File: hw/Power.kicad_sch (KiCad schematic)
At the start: 1 part, among them J4 CONN_BAT

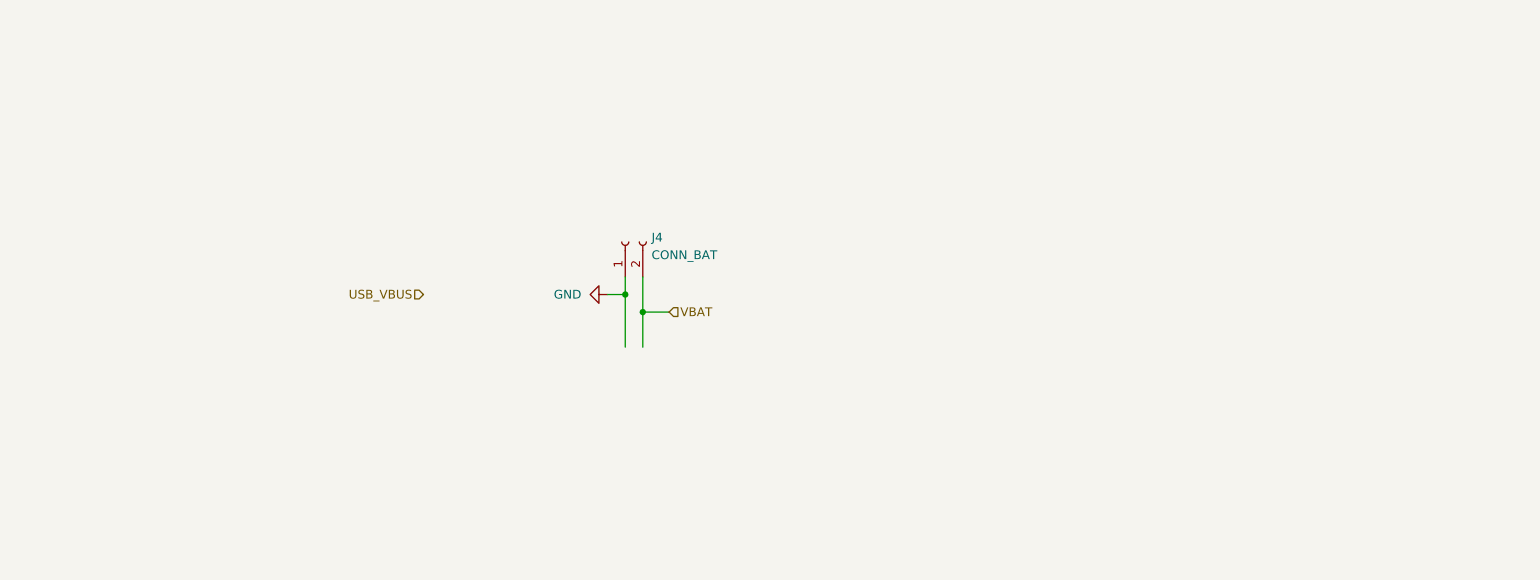
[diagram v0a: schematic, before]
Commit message: Replace case, start on Power stages
I've replaced the case STL with one that's better in every way, it prints faster, doesn't need supports, and the holder for the diffuser is better,

I may still tweak the design but I'm happy with it for now.
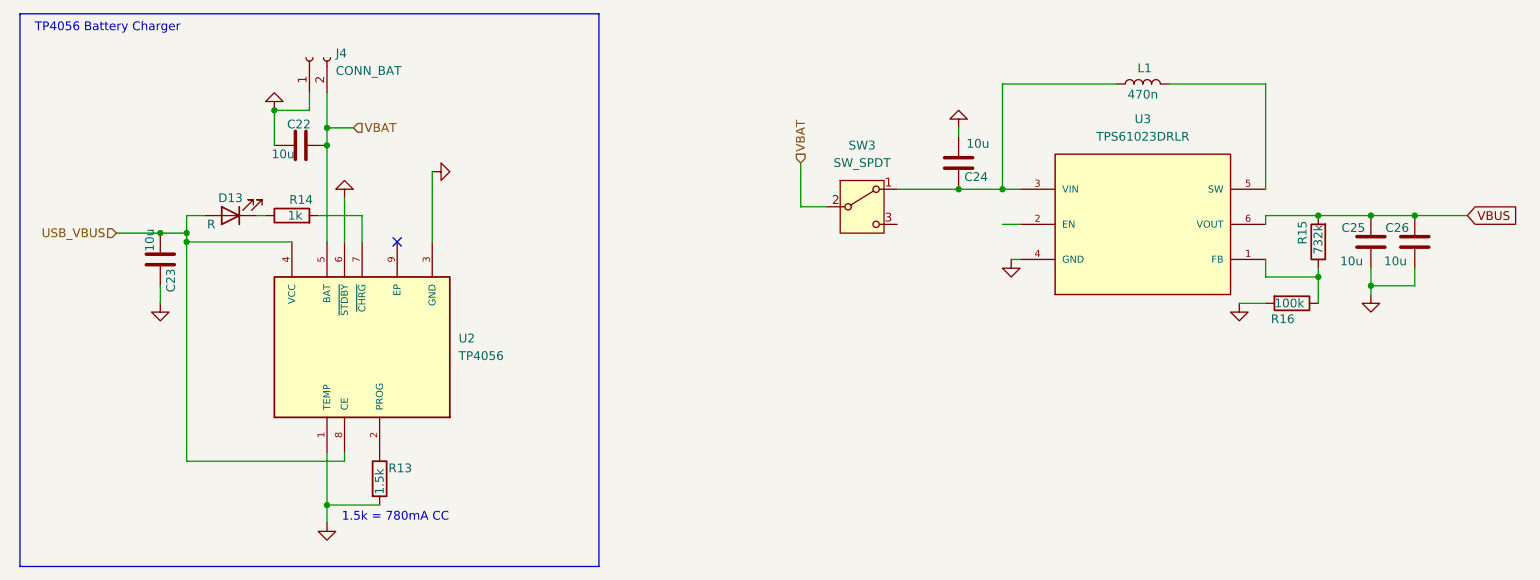
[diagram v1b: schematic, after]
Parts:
- added C22, C23, C24, C25, C26: 10u, symbol Device:C
- added D13: R, symbol Device:LED
- added L1: 470n, symbol Device:L
- added R13: 1.5k, symbol Device:R
- added R14: 1k, symbol Device:R
- added R15: 732k, symbol Device:R
- added R16: 100k, symbol Device:R
- added SW3: SW_SPDT, symbol Switch:SW_SPDT
- added U2: TP4056, TP4056:SOP127P600X175-9N, symbol TP4056:TP4056
- added U3: TPS61023DRLR, TPS61023DRLR:DRL0006A, symbol TPS61023DRLR:TPS61023DRLR
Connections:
- net GND: now also C22.2, C23.2, C24.2, C25.2, C26.2, R13.2, R16.2, U2.1 (TEMP), U2.3 (GND), U2.6 (~{STDBY}), U3.4 (GND)
- net USB_VBUS: now also C23.1, D13.2 (A), U2.4 (VCC), U2.8 (CE)
- net VBAT: now also C22.1, SW3.2 (B), U2.5 (BAT)
- new net: C24.1, L1.1, SW3.1 (A), U3.3 (VIN)
- new net: R15.1, R16.1, U3.1 (FB)
- new net: L1.2, U3.5 (SW)
- new net: D13.1 (K), R14.1
- new net: R13.1, U2.2 (PROG)
- new net: R14.2, U2.7 (~{CHRG})
- new net VBUS: C25.1, C26.1, R15.2, U3.6 (VOUT)
- no-connect marks 0 -> 1
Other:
- note added: "1.5k = 780mA CC"
- note added: "TP4056 Battery Charger"
- moved on the sheet: J4

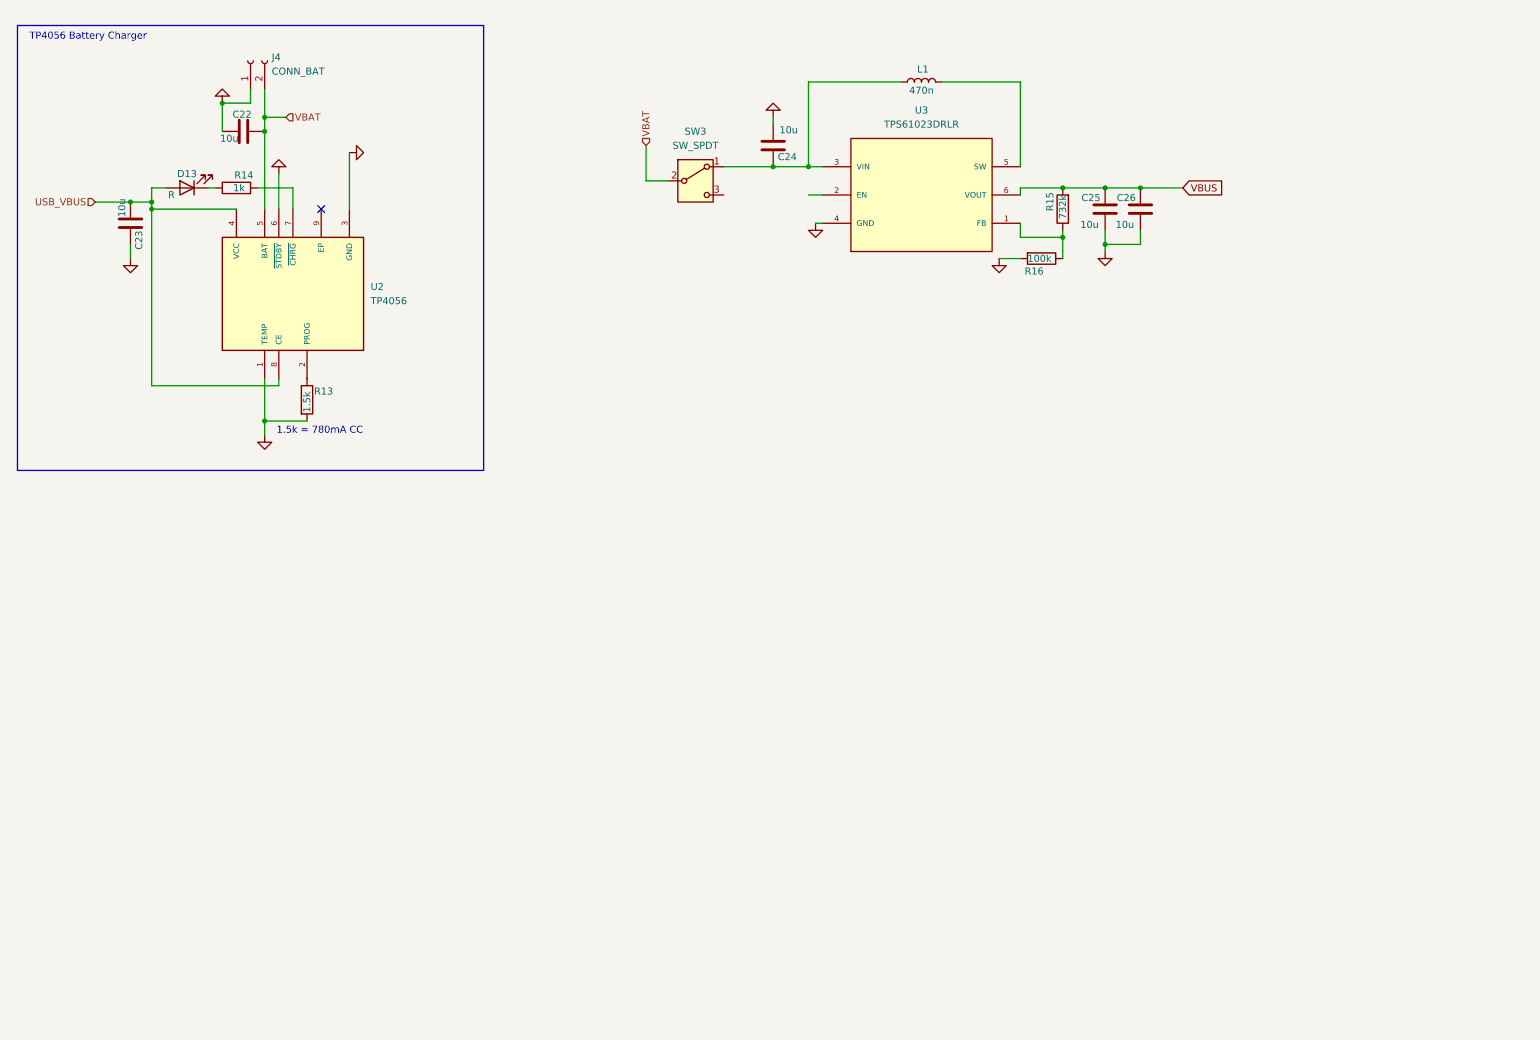
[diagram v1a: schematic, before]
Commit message: Finish power stage, work on other stages
Power stage should be finalised, I've updated LED stage to include a solder jumper, to allow up to half of the LEDs to be removed in the case of power/cost savings
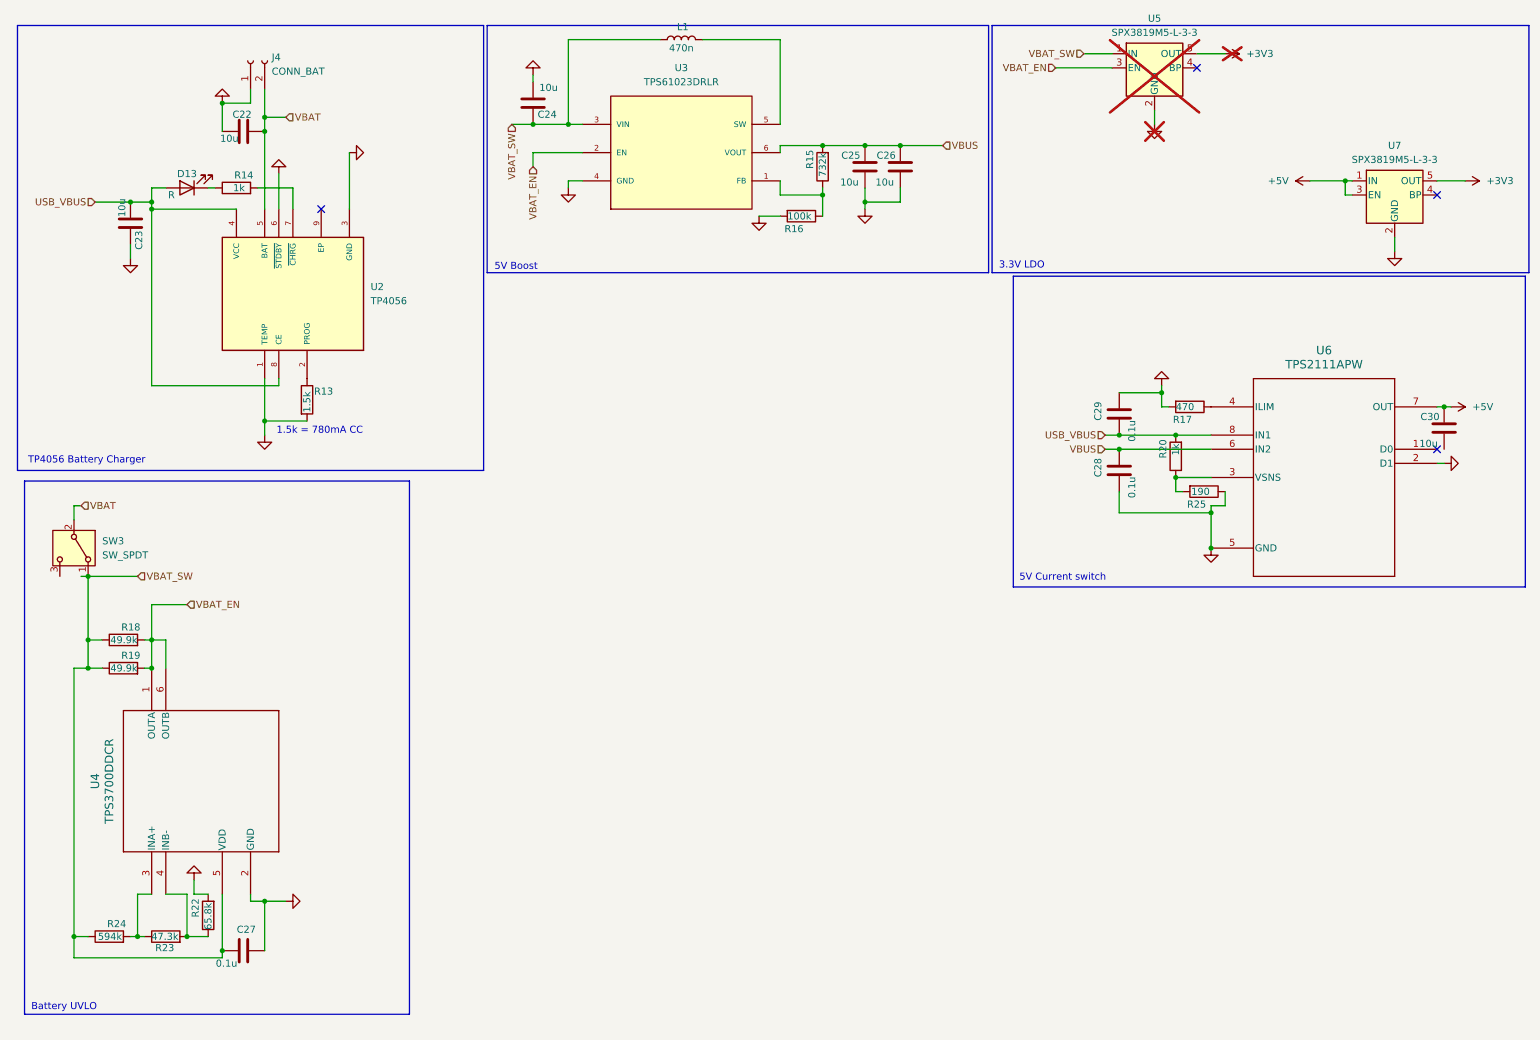
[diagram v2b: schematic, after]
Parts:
- added C27, C28, C29: 0.1u, symbol Device:C
- added C30: 10u, symbol Device:C
- added R17: 470, symbol Device:R
- added R18, R19: 49.9k, symbol Device:R
- added R20: 1k, symbol Device:R
- added R22: 65.8k, symbol Device:R
- added R23: 47.3k, symbol Device:R
- added R24: 594k, symbol Device:R
- added R25: 190, symbol Device:R
- added U4: TPS3700DDCR, DDC6_TEX, symbol TPS3700:TPS3700DDCR
- added U5, U7: SPX3819M5-L-3-3, Package_TO_SOT_SMD:SOT-23-5, symbol Regulator_Linear:SPX3819M5-L-3-3
- added U6: TPS2111APW, PW8, symbol TPS2111A:TPS2111APW
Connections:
- net GND: now also C27.2, C28.1, C29.2, R17.2, R22.2, R25.1, U4.2 (GND), U5.2 (GND), U6.2 (D1), U6.5 (GND), U7.2 (GND)
- net USB_VBUS: now also C29.1, R20.2, U6.8 (IN1)
- net VBUS: now also C28.2, U6.6 (IN2)
- net VBAT_SW: now reaches C24.1, L1.1, SW3.1 (A), U3.3 (VIN)
- net VBAT_SW: now also C27.1, R18.1, R19.1, R24.1, U4.5 (VDD), U5.1 (IN)
- net VBAT_EN: now reaches U3.2 (EN)
- net VBAT_EN: now also R18.2, R19.2, U4.1 (OUTA), U4.6 (OUTB), U5.3 (EN)
- new net: R22.1, R23.2, U4.4 (INB-)
- new net: R23.1, R24.2, U4.3 (INA+)
- new net: R20.1, R25.2, U6.3 (VSNS)
- new net: R17.1, U6.4 (ILIM)
- new net +3V3: U5.5 (OUT), U7.5 (OUT)
- new net +5V: C30.1, U6.7 (OUT), U7.1 (IN), U7.3 (EN)
- no-connect marks 1 -> 4
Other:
- note added: "3.3V LDO"
- note added: "5V Boost"
- note added: "5V Current switch"
- note added: "Battery UVLO"
- moved on the sheet: C24, C25, C26, L1, R15, R16, U3

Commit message: Work on footprinting and PCB
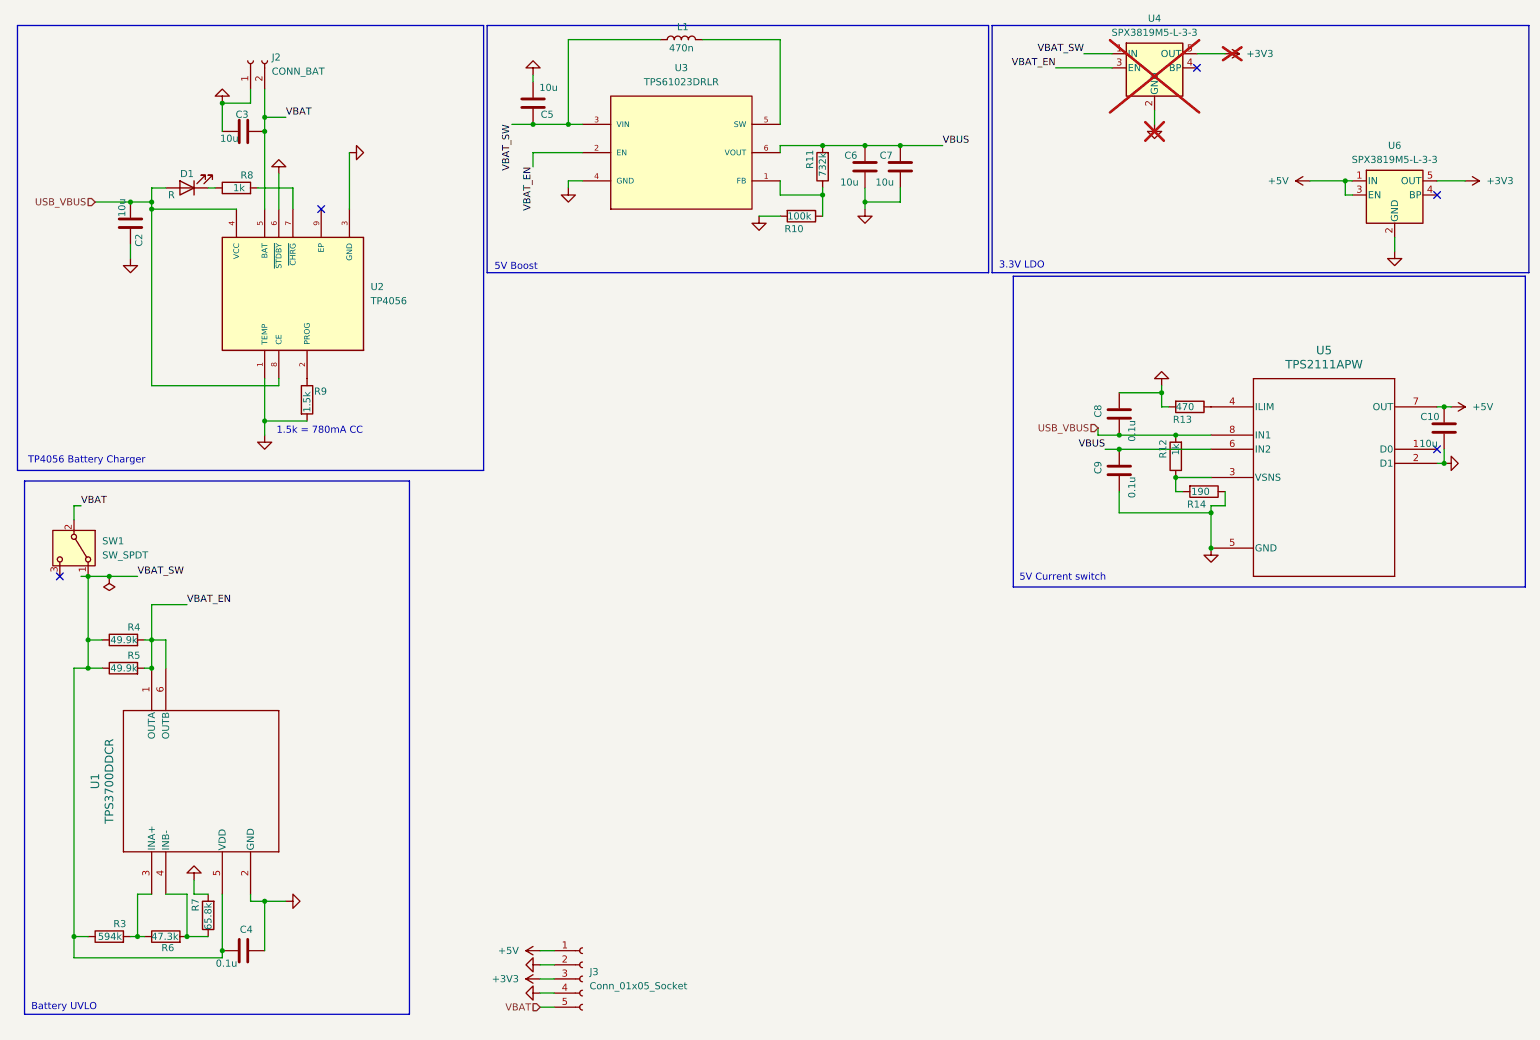
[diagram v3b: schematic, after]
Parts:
- added J3: Conn_01x05_Socket, symbol Connector:Conn_01x05_Socket
- C10: renamed from C30; footprint (none) -> Capacitor_SMD:C_0805_2012Metric_Pad1.18x1.45mm_HandSolder
- C2: renamed from C23; footprint (none) -> Capacitor_SMD:C_0805_2012Metric
- C3: renamed from C22; footprint (none) -> Capacitor_SMD:C_0805_2012Metric
- C4: renamed from C27; footprint (none) -> Capacitor_SMD:C_0603_1608Metric
- C5: renamed from C24; footprint (none) -> Capacitor_SMD:C_0805_2012Metric
- C6: renamed from C25; footprint (none) -> Capacitor_SMD:C_0805_2012Metric
- C7: renamed from C26; footprint (none) -> Capacitor_SMD:C_0805_2012Metric
- C8: renamed from C29; footprint (none) -> Capacitor_SMD:C_0603_1608Metric
- C9: renamed from C28; footprint (none) -> Capacitor_SMD:C_0603_1608Metric
- SW1: renamed from SW3; footprint (none) -> Button_Switch_THT:SW_Slide_SPDT_Straight_CK_OS102011MS2Q
- U1: renamed from U4; footprint DDC6_TEX -> lib:DDC6_TEX-M
- U5: renamed from U6; footprint PW8 -> lib:PW8
- renumbered D13 to D1, J4 to J2, R16 to R10, R15 to R11, R20 to R12, R17 to R13, R25 to R14, R24 to R3, R18 to R4, R19 to R5, R23 to R6, R22 to R7, R14 to R8, R13 to R9, U5 to U4, U7 to U6
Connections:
- net +3V3: now also J3.3 (Pin_3)
- net +5V: now also J3.1 (Pin_1)
- net GND: now also C10.2, J3.2 (Pin_2), J3.4 (Pin_4)
- net VBAT: now also J3.5 (Pin_5)
- no-connect marks 4 -> 5
